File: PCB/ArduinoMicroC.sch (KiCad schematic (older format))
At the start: 28 parts, among them J1 USB_C_Receptacle_USB2.0, J2 Conn_01x12, J3 Conn_01x06, J4 Conn_01x12, SW1 SW_Check_USB, SW2 SW_Push, U1 MIC5219-5.0YM5, U2 ATmega32U4-MU, Y1 16MHz

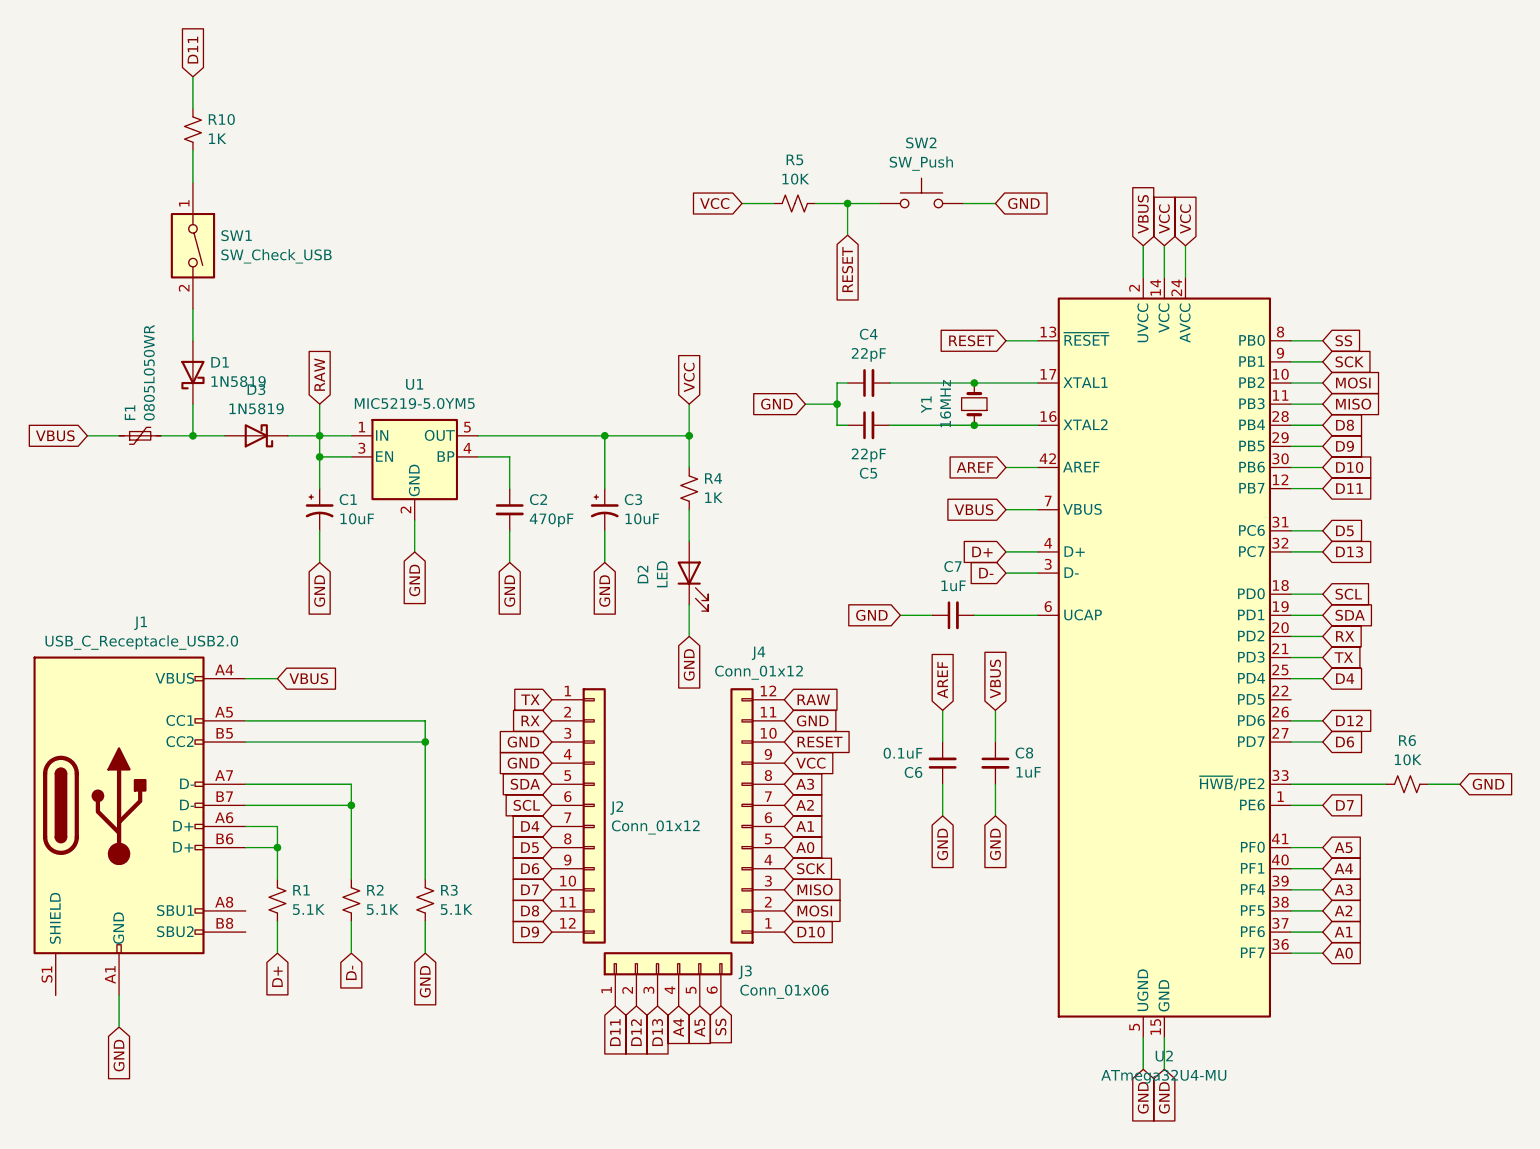
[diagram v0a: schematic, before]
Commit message: Second version of PCB
- Make D11 pin is USB check pin only.
- Remove D11 out of GPIO headers.
- Remove TX LED and RX LED.
- Smaller PCB with 29 pins instead of 30 pins.
- Fix the USB check diode.
- Add a Resistor to GND in D11 pin.
- Use USB-C 2.0 connector instead of 3.0.
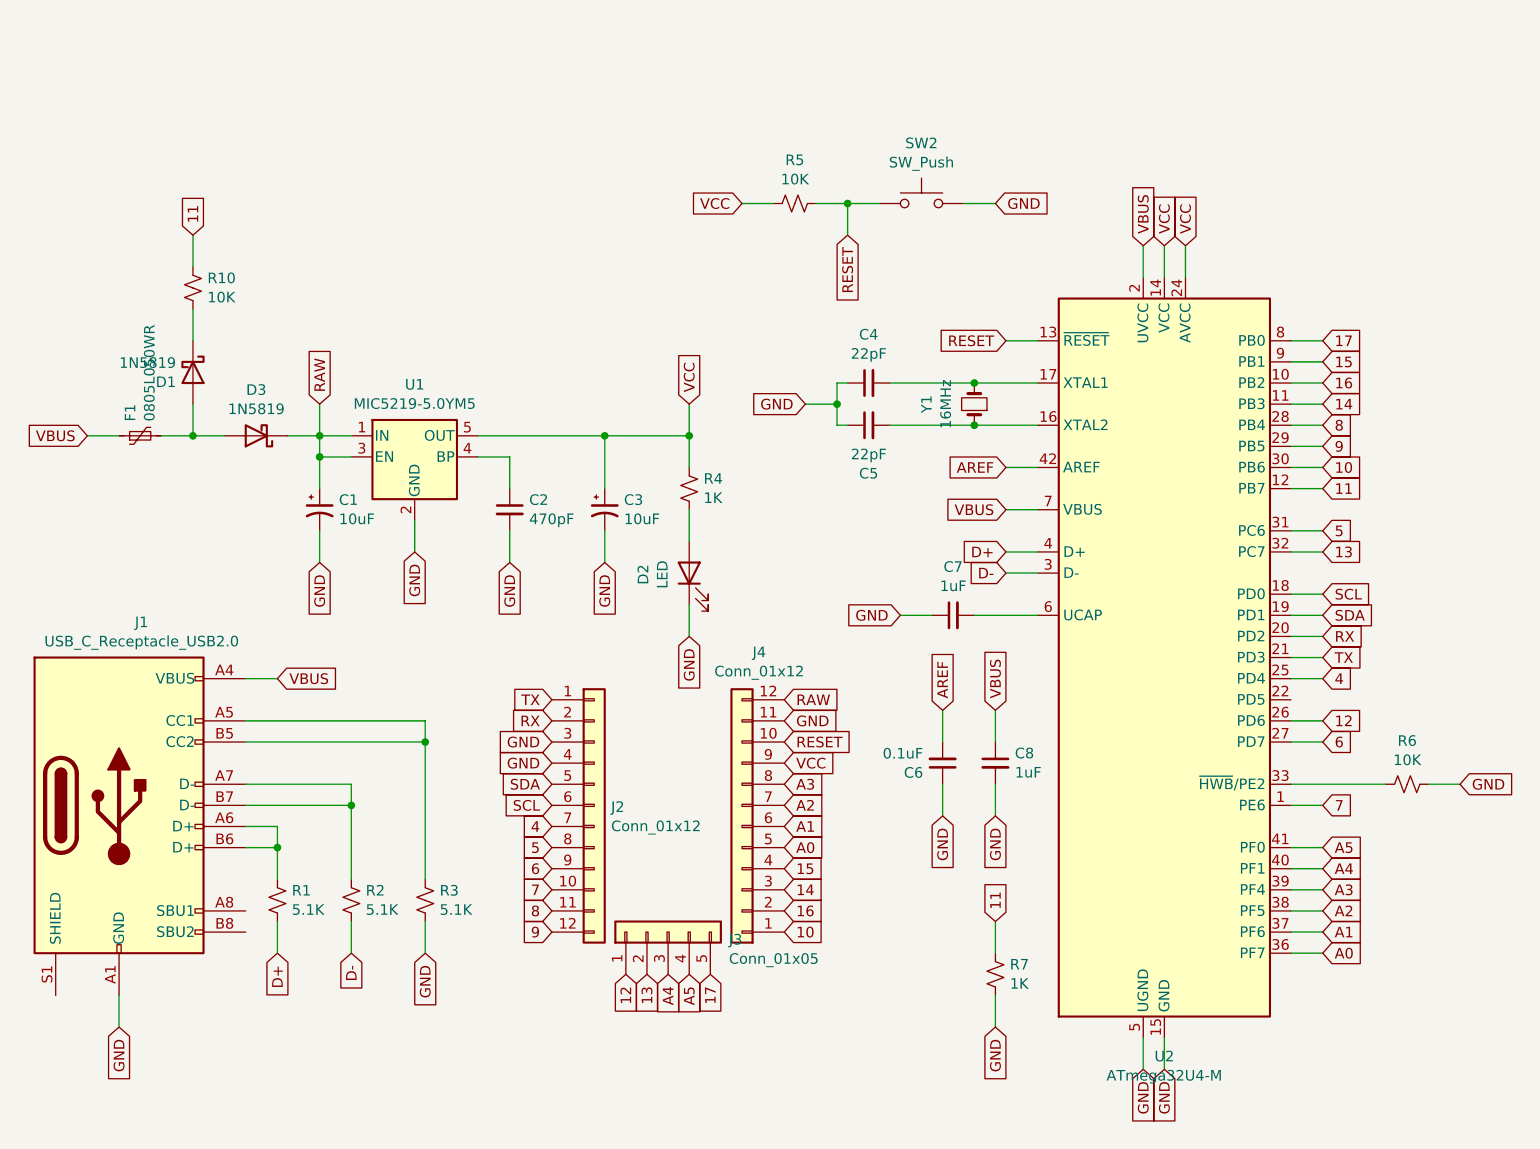
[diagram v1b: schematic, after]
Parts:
- removed J3: Conn_01x06, NeihConnector:PinHeader_1x06_P2.54mm_Circular_Vertical_2, symbol Connector_Generic:Conn_01x06
- removed SW1: SW_Check_USB, Button_Switch_SMD:SW_DIP_SPSTx01_Slide_Copal_CVS-01xB_W5.9mm_P1mm, symbol Switch:SW_DIP_x01
- removed U2: ATmega32U4-MU, NeihPackage:QFN-44-1EP_7x7mm_P0.5mm_EP5.2x5.2mm, symbol MCU_Microchip_ATmega:ATmega32U4-MU
- added J3: Conn_01x05, NeihConnector:PinHeader_1x05_P2.54mm_Circular_Vertical_2, symbol Connector_Generic:Conn_01x05
- added R7: 1K, Resistor_SMD:R_0201_0603Metric, symbol Device:R_Small_US
- added U2: ATmega32U4-M, Package_DFN_QFN:QFN-44-1EP_7x7mm_P0.5mm_EP5.2x5.2mm, symbol MCU_Microchip_ATmega:ATmega32U4-M
- J1: footprint Connector_USB:USB_C_Receptacle_Amphenol_12401610E4-2A -> Connector_USB:USB_C_Receptacle_HRO_TYPE-C-31-M-12
- R10: value 1K -> 10K
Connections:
- net A0: now also U2.36 (PF7)
- net A1: now also U2.37 (PF6)
- net A2: now also U2.38 (PF5)
- net A3: now also U2.39 (PF4)
- net A4: now also J3.3 (Pin_3), U2.40 (PF1)
- net A5: now also J3.4 (Pin_4), U2.41 (PF0)
- net AREF: now also U2.42 (AREF)
- net D+: now also U2.4 (D+)
- net D-: now also U2.3 (D-)
- net GND: now also R7.2, U2.15 (GND), U2.23 (GND), U2.35 (GND), U2.43 (GND), U2.45 (GND), U2.5 (UGND)
- net RESET: now also U2.13 (~RESET)
- net RX: now also U2.20 (PD2)
- net SCL: now also U2.18 (PD0)
- net SDA: now also U2.19 (PD1)
- net TX: now also U2.21 (PD3)
- net VBUS: now also U2.2 (UVCC), U2.7 (VBUS)
- net VCC: now also U2.14 (VCC), U2.24 (AVCC), U2.34 (VCC), U2.44 (AVCC)
- net at C5.2, Y1.1: now also U2.16 (XTAL2)
- net at C4.2, Y1.2: now also U2.17 (XTAL1)
- net at C7.2: now also U2.6 (UCAP)
- net at R6.1: now also U2.33 (~HWB~/PE2)
- net at D3.2 (A), F1.2: now also D1.2 (A); no longer D1.1 (K)
- net at R10.2: now also D1.1 (K)
- net D10 renamed 10
- net 10: now also U2.30 (PB6)
- net D11 renamed 11
- net 11: now also R7.1, U2.12 (PB7)
- net D4 renamed 4
- net 4: now also U2.25 (PD4)
- net D5 renamed 5
- net 5: now also U2.31 (PC6)
- net D6 renamed 6
- net 6: now also U2.27 (PD7)
- net D7 renamed 7
- net 7: now also U2.1 (PE6)
- net D8 renamed 8
- net 8: now also U2.28 (PB4)
- net D9 renamed 9
- net 9: now also U2.29 (PB5)
- net MISO renamed 14
- net 14: now also U2.11 (PB3)
- net MOSI renamed 16
- net 16: now also U2.10 (PB2)
- net SCK renamed 15
- net 15: now also U2.9 (PB1)
- new net 12: J3.1 (Pin_1), U2.26 (PD6)
- new net 13: J3.2 (Pin_2), U2.32 (PC7)
- new net 17: J3.5 (Pin_5), U2.8 (PB0)
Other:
- moved on the sheet: R10
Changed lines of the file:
@@
 A0
 Text GLabel 8750 2500 2    50   Input ~ 0
-SCK
+15
 Text GLabel 8750 2700 2    50   Input ~ 0
-MISO
+14
 Text GLabel 8750 2800 2    50   Input ~ 0
-D8
+8
 Text GLabel 8750 2900 2    50   Input ~ 0
-D9
+9
 Text GLabel 8750 3000 2    50   Input ~ 0
-D10
+10
 Text GLabel 8750 3100 2    50   Input ~ 0
-D11
+11
 Text GLabel 8750 3300 2    50   Input ~ 0
-D5
+5
 Wire Wire Line
 	6950 4300 6950 4150
@@
 TX
 Text GLabel 8750 4000 2    50   Input ~ 0
-D4
+4
 Text GLabel 8750 4200 2    50   Input ~ 0
-D12
+12
 Text GLabel 8750 4300 2    50   Input ~ 0
-D6
+6
 Text GLabel 8750 4600 2    50   Input ~ 0
-D7
+7
 Text GLabel 8750 2600 2    50   Input ~ 0
-MOSI
+16
 Wire Wire Line
 	3050 5500 3050 5650
@@
 	6900 3700 6750 3700
 Wire Wire Line
-	3400 1300 3400 1150
-$Comp
-L Switch:SW_DIP_x01 SW1
-U 1 1 5FBA00D1
-P 3400 1950
-F 0 "SW1" V 3354 2080 50  0000 L CNN
-F 1 "SW_Check_USB" V 3445 2080 50  0000 L CNN
-F 2 "Button_Switch_SMD:SW_DIP_SPSTx01_Slide_Copal_CVS-01xB_W5.9mm_P1mm" H 3400 1950 50  0001 C CNN
-F 3 "~" H 3400 1950 50  0001 C CNN
-	1    3400 1950
-	0    1    1    0
-$EndComp
-Text GLabel 3400 1150 1    50   Input ~ 0
-D11
+	3400 2050 3400 1900
+Text GLabel 3400 1900 1    50   Input ~ 0
+11
 Wire Wire Line
 	3400 2850 3550 2850
@@
 	5750 2850 5750 3000
 Connection ~ 5750 2850
-Connection ~ 5350 2850
 Wire Wire Line
 	5350 2850 5750 2850
@@
 Wire Wire Line
 	5350 2850 5350 3100
-Wire Wire Line
-	4750 2850 5350 2850
 Wire Wire Line
 	4900 3300 4900 3450
@@
 	4000 2950 4000 2850
 Connection ~ 4000 2950
-Wire Wire Line
-	4150 2950 4000 2950
-Wire Wire Line
-	4000 2850 4150 2850
 Connection ~ 4000 2850
 Wire Wire Line
@@
 Wire Wire Line
 	4450 3250 4450 3400
-$Comp
-L Regulator_Linear:MIC5219-5.0YM5 U1
-U 1 1 5FBA006E
-P 4450 2950
-F 0 "U1" H 4450 3292 50  0000 C CNN
-F 1 "MIC5219-5.0YM5" H 4450 3201 50  0000 C CNN
-F 2 "Package_TO_SOT_SMD:SOT-23-5" H 4450 3275 50  0001 C CNN
-F 3 "http://ww1.microchip.com/downloads/en/DeviceDoc/MIC5219-500mA-Peak-Output-LDO-Regulator-DS20006021A.pdf" H 4450 2950 50  0001 C CNN
-	1    4450 2950
-	1    0    0    -1
-$EndComp
 Wire Wire Line
 	5750 2700 5750 2850
@@
 F 0 "J1" H 3157 5467 50  0000 C CNN
 F 1 "USB_C_Receptacle_USB2.0" H 3157 5376 50  0000 C CNN
-F 2 "Connector_USB:USB_C_Receptacle_Amphenol_12401610E4-2A" H 3200 4600 50  0001 C CNN
+F 2 "Connector_USB:USB_C_Receptacle_HRO_TYPE-C-31-M-12" H 3200 4600 50  0001 C CNN
 F 3 "https://www.usb.org/sites/default/files/documents/usb_type-c.zip" H 3200 4600 50  0001 C CNN
 	1    3050 4600
@@
 L Device:R_Small_US R10
 U 1 1 5FBD8F59
-P 3400 1400
-F 0 "R10" H 3468 1446 50  0000 L CNN
-F 1 "1K" H 3468 1355 50  0000 L CNN
-F 2 "Resistor_SMD:R_0201_0603Metric" H 3400 1400 50  0001 C CNN
-F 3 "~" H 3400 1400 50  0001 C CNN
-	1    3400 1400
-	1    0    0    -1
-$EndComp
-Wire Wire Line
-	3400 1650 3400 1500
+P 3400 2150
+F 0 "R10" H 3468 2196 50  0000 L CNN
+F 1 "10K" H 3468 2105 50  0000 L CNN
+F 2 "Resistor_SMD:R_0201_0603Metric" H 3400 2150 50  0001 C CNN
+F 3 "~" H 3400 2150 50  0001 C CNN
+	1    3400 2150
+	1    0    0    -1
+$EndComp
 Wire Wire Line
 	7100 3700 7400 3700
@@
 	7400 2400 7250 2400
 Text GLabel 8750 3400 2    50   Input ~ 0
-D13
+13
 Text GLabel 8750 2400 2    50   Input ~ 0
-SS
+17
 Wire Wire Line
 	8600 5300 8750 5300
@@
 	0    -1   -1   0
 $EndComp
-$Comp
-L MCU_Microchip_ATmega:ATmega32U4-MU U2
-U 1 1 5FB9FFDE
-P 8000 3900
-F 0 "U2" H 8000 2011 50  0000 C CNN
-F 1 "ATmega32U4-MU" H 8000 1920 50  0000 C CNN
-F 2 "NeihPackage:QFN-44-1EP_7x7mm_P0.5mm_EP5.2x5.2mm" H 8000 3900 50  0001 C CIN
-F 3 "http://ww1.microchip.com/downloads/en/DeviceDoc/Atmel-7766-8-bit-AVR-ATmega16U4-32U4_Datasheet.pdf" H 8000 3900 50  0001 C CNN
-	1    8000 3900
-	1    0    0    -1
-$EndComp
 Text GLabel 6000 1750 0    50   Input ~ 0
 VCC
@@
 	1    5300 4600
 	1    0    0    -1
-$EndComp
-$Comp
-L Connector_Generic:Conn_01x06 J3
-U 1 1 5FC6CBBF
-P 5600 5350
-F 0 "J3" V 5564 4962 50  0000 R CNN
-F 1 "Conn_01x06" V 5473 4962 50  0000 R CNN
-F 2 "NeihConnector:PinHeader_1x06_P2.54mm_Circular_Vertical_2" H 5600 5350 50  0001 C CNN
-F 3 "~" H 5600 5350 50  0001 C CNN
-	1    5600 5350
-	0    -1   -1   0
 $EndComp
 $Comp
@@
 SCL
 Text GLabel 5100 4700 0    50   Input ~ 0
-D4
+4
 Text GLabel 5100 4800 0    50   Input ~ 0
-D5
+5
 Text GLabel 5100 4900 0    50   Input ~ 0
-D6
+6
 Text GLabel 5100 5000 0    50   Input ~ 0
-D7
+7
 Text GLabel 5100 5100 0    50   Input ~ 0
-D8
+8
 Text GLabel 5100 5200 0    50   Input ~ 0
-D9
+9
 Text GLabel 6200 4100 2    50   Input ~ 0
 RAW
@@
 A0
 Text GLabel 6200 4900 2    50   Input ~ 0
-SCK
+15
 Text GLabel 6200 5000 2    50   Input ~ 0
-MISO
+14
 Text GLabel 6200 5100 2    50   Input ~ 0
-MOSI
+16
 Text GLabel 6200 5200 2    50   Input ~ 0
-D10
-Text GLabel 5400 5550 3    50   Input ~ 0
-D11
-Text GLabel 5500 5550 3    50   Input ~ 0
-D12
-Text GLabel 5600 5550 3    50   Input ~ 0
-D13
-Text GLabel 5700 5550 3    50   Input ~ 0
+10
+Text GLabel 5450 5400 3    50   Input ~ 0
+12
+Text GLabel 5550 5400 3    50   Input ~ 0
+13
+Text GLabel 5650 5400 3    50   Input ~ 0
 A4
-Text GLabel 5800 5550 3    50   Input ~ 0
+Text GLabel 5750 5400 3    50   Input ~ 0
 A5
-Text GLabel 5900 5550 3    50   Input ~ 0
-SS
+Text GLabel 5850 5400 3    50   Input ~ 0
+17
 $Comp
 L Diode:1N5819 D3
@@
 F 3 "http://www.vishay.com/docs/88525/1n5817.pdf" H 3400 2550 50  0001 C CNN
 	1    3400 2550
+	0    1    1    0
+$EndComp
+Wire Wire Line
+	3400 2400 3400 2250
+$Comp
+L Connector_Generic:Conn_01x05 J3
+U 1 1 5FDE6139
+P 5650 5200
+F 0 "J3" V 5614 4912 50  0000 R CNN
+F 1 "Conn_01x05" V 5523 4912 50  0000 R CNN
+F 2 "NeihConnector:PinHeader_1x05_P2.54mm_Circular_Vertical_2" H 5650 5200 50  0001 C CNN
+F 3 "~" H 5650 5200 50  0001 C CNN
+	1    5650 5200
 	0    -1   -1   0
 $EndComp
-Wire Wire Line
-	3400 2400 3400 2250
+$Comp
+L MCU_Microchip_ATmega:ATmega32U4-M U2
+U 1 1 5FE010D0
+P 8000 3900
+F 0 "U2" H 8000 2011 50  0000 C CNN
+F 1 "ATmega32U4-M" H 8000 1920 50  0000 C CNN
+F 2 "Package_DFN_QFN:QFN-44-1EP_7x7mm_P0.5mm_EP5.2x5.2mm" H 8000 3900 50  0001 C CIN
+F 3 "http://ww1.microchip.com/downloads/en/DeviceDoc/Atmel-7766-8-bit-AVR-ATmega16U4-32U4_Datasheet.pdf" H 8000 3900 50  0001 C CNN
+	1    8000 3900
+	1    0    0    -1
+$EndComp
+Text GLabel 7200 5150 1    50   Input ~ 0
+11
+Text GLabel 7200 5650 3    50   Input ~ 0
+GND
+$Comp
+L Device:R_Small_US R7
+U 1 1 5FEB92E9
+P 7200 5400
+F 0 "R7" H 7268 5446 50  0000 L CNN
+F 1 "1K" H 7268 5355 50  0000 L CNN
+F 2 "Resistor_SMD:R_0201_0603Metric" H 7200 5400 50  0001 C CNN
+F 3 "~" H 7200 5400 50  0001 C CNN
+	1    7200 5400
+	1    0    0    -1
+$EndComp
+Wire Wire Line
+	7200 5150 7200 5300
+Wire Wire Line
+	7200 5500 7200 5650
+Connection ~ 5350 2850
+Wire Wire Line
+	4150 2950 4000 2950
+Wire Wire Line
+	4000 2850 4150 2850
+$Comp
+L Regulator_Linear:MIC5219-5.0YM5 U1
+U 1 1 5FBA006E
+P 4450 2950
+F 0 "U1" H 4450 3292 50  0000 C CNN
+F 1 "MIC5219-5.0YM5" H 4450 3201 50  0000 C CNN
+F 2 "Package_TO_SOT_SMD:SOT-23-5" H 4450 3275 50  0001 C CNN
+F 3 "http://ww1.microchip.com/downloads/en/DeviceDoc/MIC5219-500mA-Peak-Output-LDO-Regulator-DS20006021A.pdf" H 4450 2950 50  0001 C CNN
+	1    4450 2950
+	1    0    0    -1
+$EndComp
+Wire Wire Line
+	4750 2850 5350 2850
 $EndSCHEMATC

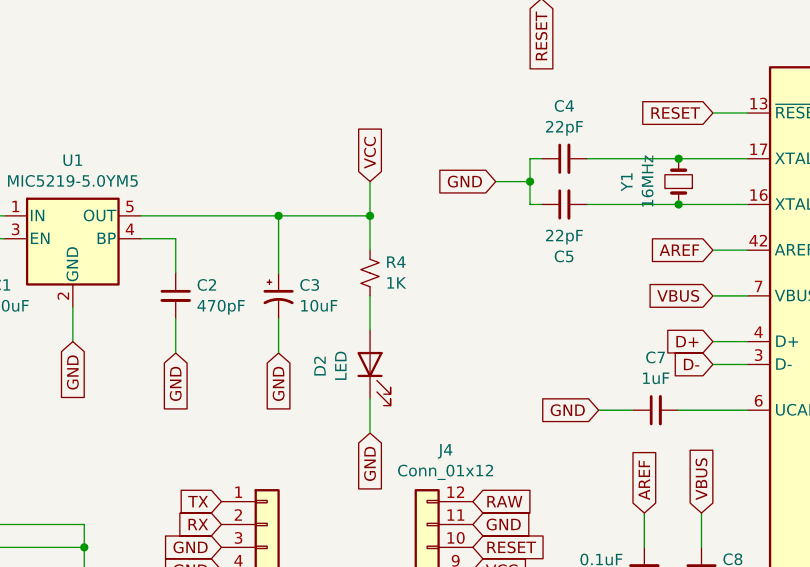
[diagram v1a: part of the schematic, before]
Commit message: Make zone outline for USB Sheld and update module library and footprint for new version
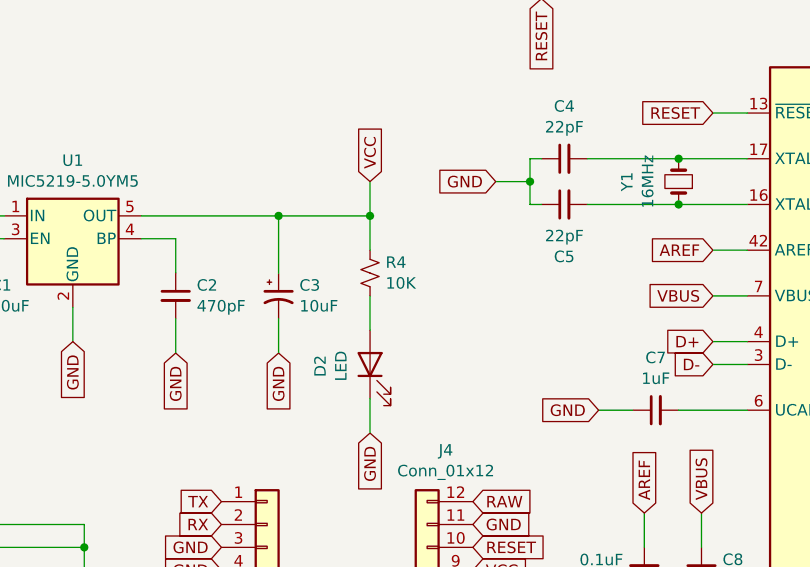
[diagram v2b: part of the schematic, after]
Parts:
- R4: value 1K -> 10K
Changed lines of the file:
@@
 P 5750 3100
 F 0 "R4" H 5818 3146 50  0000 L CNN
-F 1 "1K" H 5818 3055 50  0000 L CNN
+F 1 "10K" H 5818 3055 50  0000 L CNN
 F 2 "Resistor_SMD:R_0201_0603Metric" H 5750 3100 50  0001 C CNN
 F 3 "~" H 5750 3100 50  0001 C CNN
